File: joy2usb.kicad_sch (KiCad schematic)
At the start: 14 parts, among them J1 DB9_Male, J2 Conn_02x04_Odd_Even, SW1 RST, SW2 SW_SPDT, U1 Arduino_Pro_Micro, U2 4066

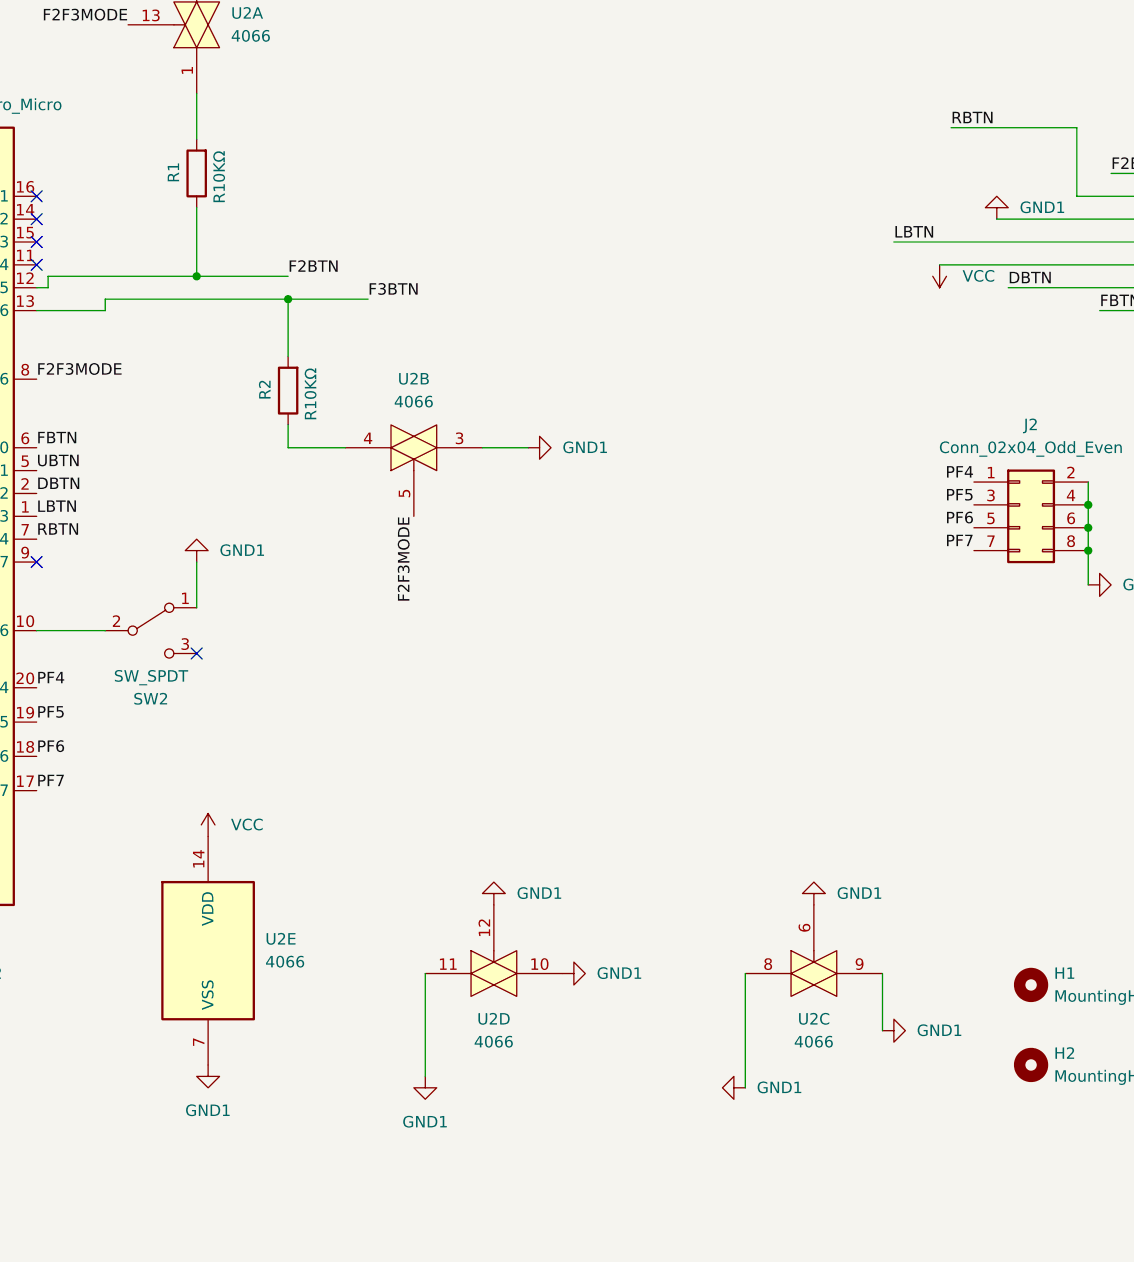
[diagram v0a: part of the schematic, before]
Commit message: PCB Rev. 2.0
Diode D1 is turned on in the same way as PULL-DOWN for the C64 Mode. Thus when D1 is on it means that PULL-DOWN for the C64 Mode is on, too.
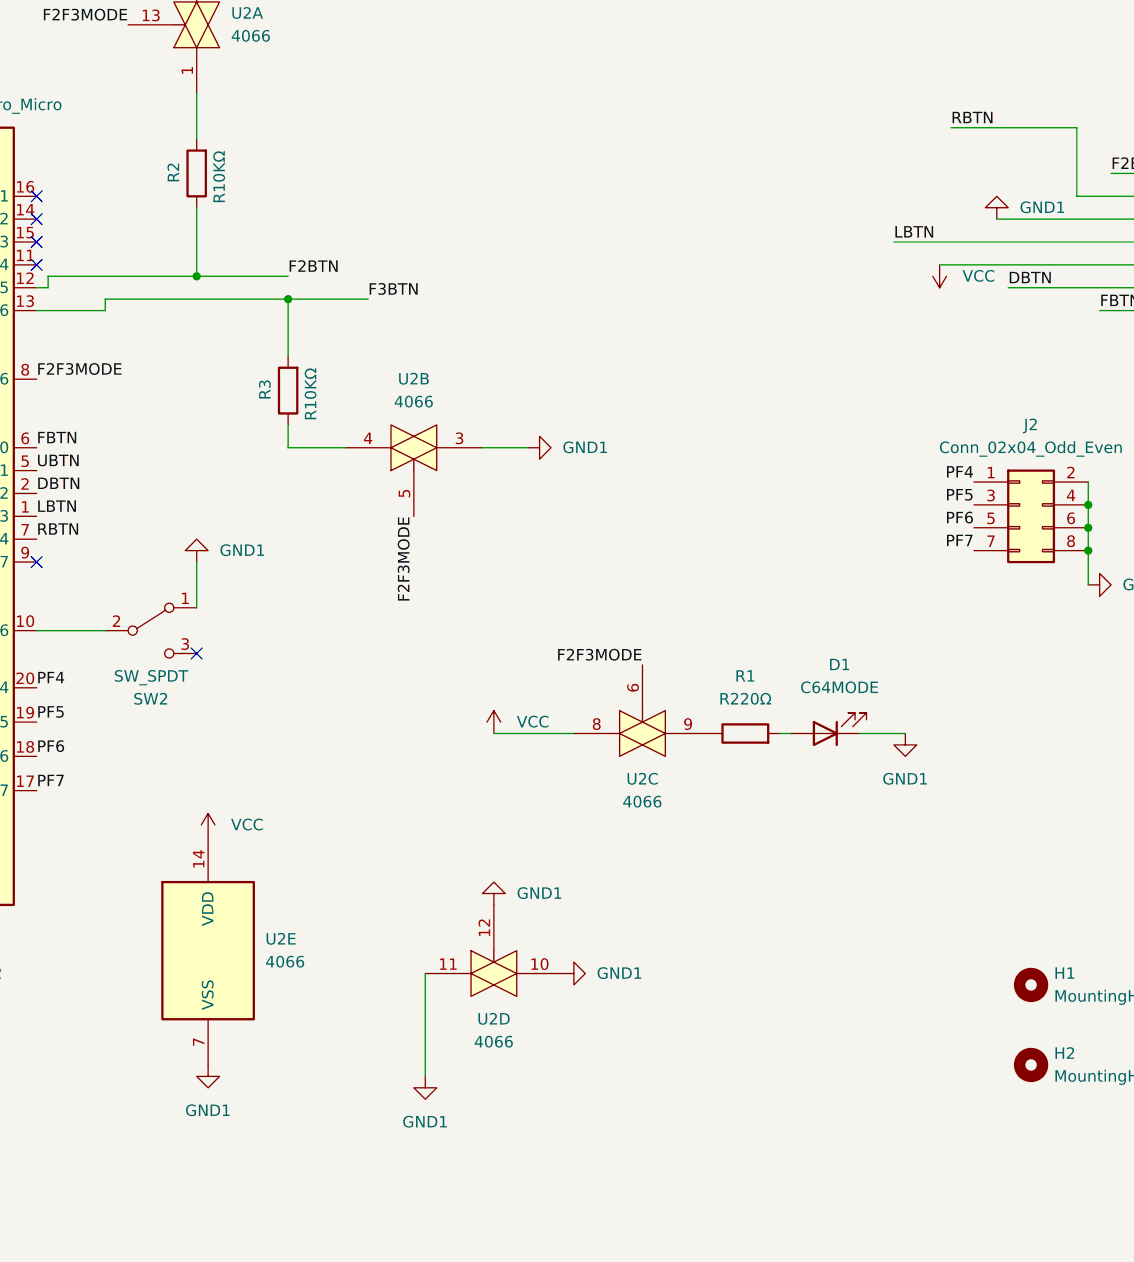
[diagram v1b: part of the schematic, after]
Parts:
- added D1: C64MODE, LED_THT:LED_D4.0mm, symbol Device:LED
- added R1: R220Ω, Resistor_THT:R_Axial_DIN0207_L6.3mm_D2.5mm_P10.16mm_Horizontal, symbol Device:R
- renumbered R1 to R2, R2 to R3
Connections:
- net F2F3MODE: now also U2.6
- net GND1: now also D1.1 (K); no longer U2.6, U2.8, U2.9
- net VCC: now also U2.8
- new net: R1.1, U2.9
- new net: D1.2 (A), R1.2

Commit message: PCB Rev. 2.3
Update of footprints -- oval pads
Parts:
- J1: footprint Connector_Dsub:DSUB-9_Male_Horizontal_P2.77x2.84mm_EdgePinOffset9.90mm_Housed_MountingHolesOffset11.32mm -> Misc:DSUB-9_Male_Horizontal_P2.77x2.84mm_EdgePinOffset9.90mm_Housed_OVAL_MountingHolesOffset11.32mm
- SW2: footprint Misc:MFP_1220_KNITTER_SWITCH_SPDT -> Misc:MFP_1220_KNITTER_SWITCH_SPDT_Oval
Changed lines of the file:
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@@
     (property "Reference" "SW2" (id 0) (at 124.46 106.68 0))
     (property "Value" "SW_SPDT" (id 1) (at 124.46 104.14 0))
-    (property "Footprint" "Misc:MFP_1220_KNITTER_SWITCH_SPDT" (id 2) (at 124.46 99.06 0)
+    (property "Footprint" "Misc:MFP_1220_KNITTER_SWITCH_SPDT_Oval" (id 2) (at 124.46 99.06 0)
       (effects (font (size 1.27 1.27)) hide)
     )
@@
       (effects (font (size 1.27 1.27)) (justify left))
     )
-    (property "Footprint" "Connector_Dsub:DSUB-9_Male_Horizontal_P2.77x2.84mm_EdgePinOffset9.90mm_Housed_MountingHolesOffset11.32mm" (id 2) (at 246.38 55.88 0)
+    (property "Footprint" "Misc:DSUB-9_Male_Horizontal_P2.77x2.84mm_EdgePinOffset9.90mm_Housed_OVAL_MountingHolesOffset11.32mm" (id 2) (at 246.38 55.88 0)
       (effects (font (size 1.27 1.27)) hide)
     )
@@
     )
     (path "/904b9dce-e0fa-4996-95ed-5106b4f66a12"
-      (reference "J1") (unit 1) (value "DB9_Male") (footprint "Connector_Dsub:DSUB-9_Male_Horizontal_P2.77x2.84mm_EdgePinOffset9.90mm_Housed_MountingHolesOffset11.32mm")
+      (reference "J1") (unit 1) (value "DB9_Male") (footprint "Misc:DSUB-9_Male_Horizontal_P2.77x2.84mm_EdgePinOffset9.90mm_Housed_OVAL_MountingHolesOffset11.32mm")
     )
     (path "/aa99628a-edde-4438-a929-0fc1f87b7e93"
@@
     )
     (path "/0dcce0bd-aa77-40a7-aa11-13358cb7d8b3"
-      (reference "SW2") (unit 1) (value "SW_SPDT") (footprint "Misc:MFP_1220_KNITTER_SWITCH_SPDT")
+      (reference "SW2") (unit 1) (value "SW_SPDT") (footprint "Misc:MFP_1220_KNITTER_SWITCH_SPDT_Oval")
     )
     (path "/5402cd64-4343-4e58-a540-d14fb99563fb"

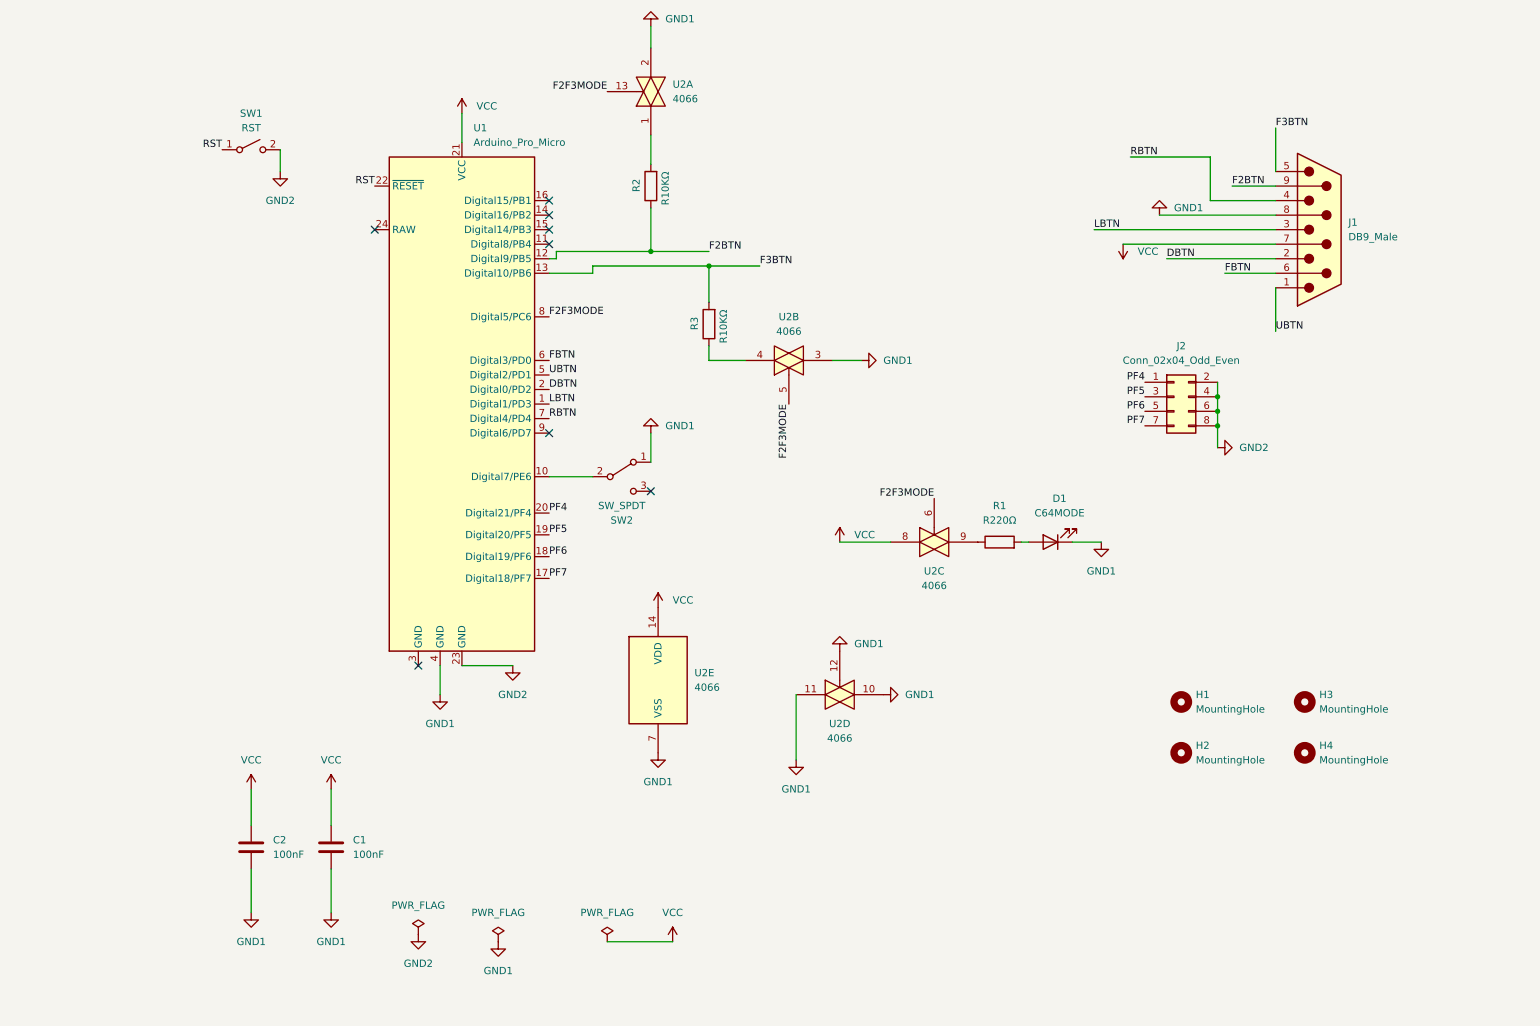
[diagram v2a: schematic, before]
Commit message: PCB Rev. 2.5
Update of LED footprint
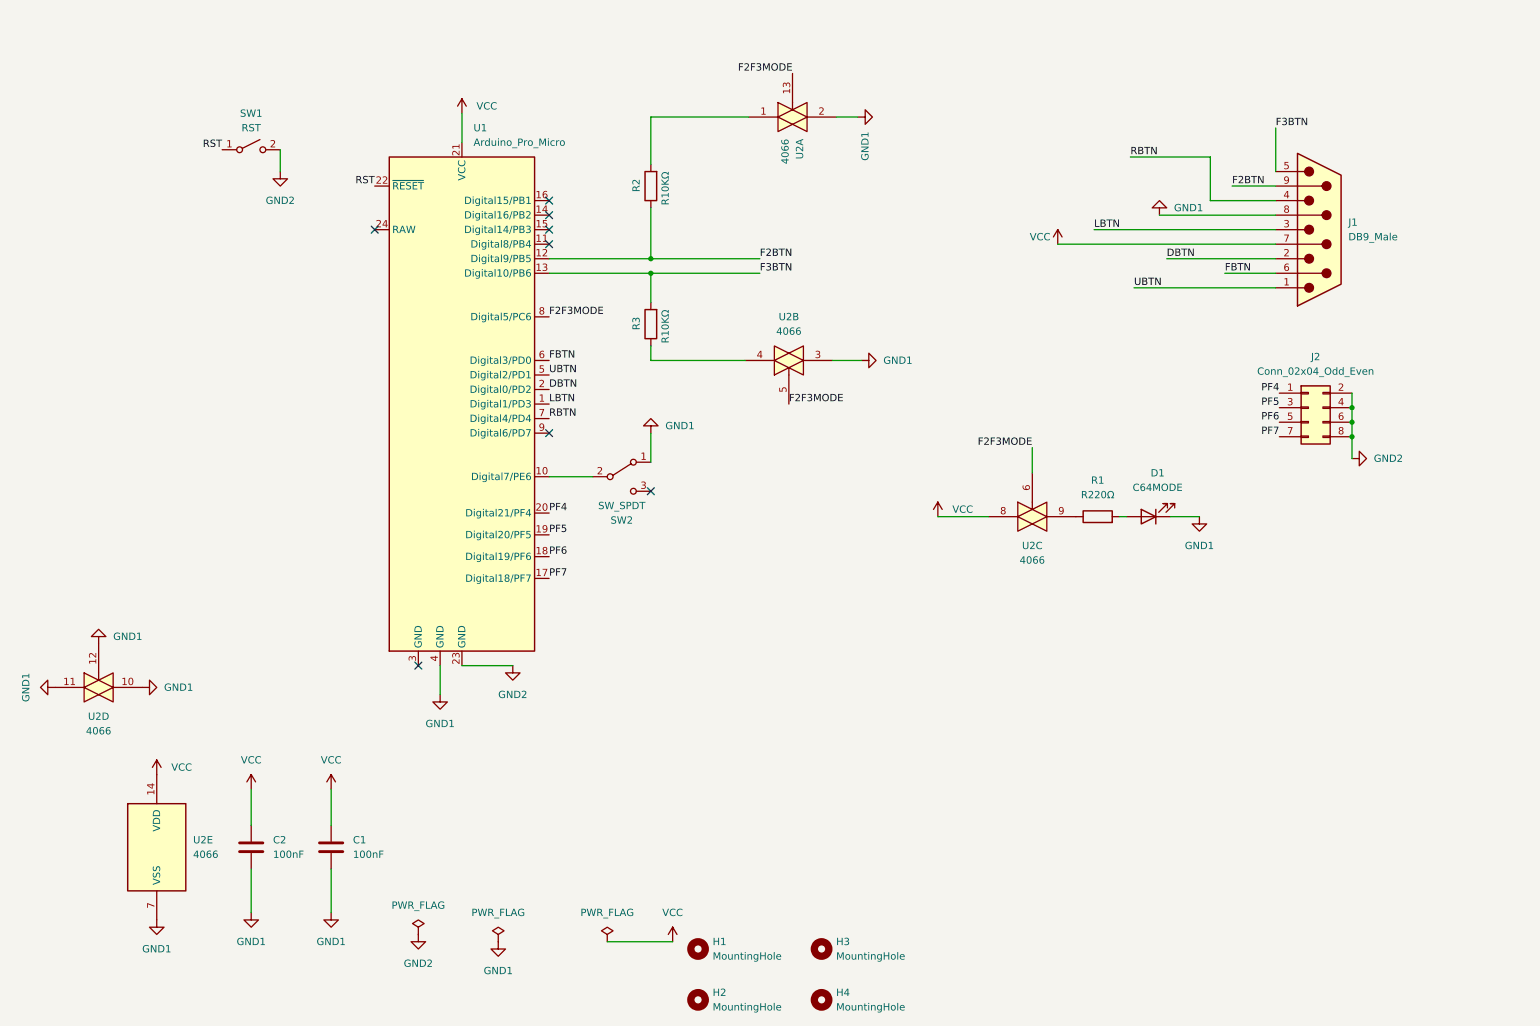
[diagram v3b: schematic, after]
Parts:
- D1: footprint LED_THT:LED_D4.0mm -> Misc:LED_D3.0mm_Oval
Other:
- moved on the sheet: D1, H1, H2, H3, H4, J2, R1, R3, U2A, U2C, U2D, U2E

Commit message: PCB Rev. 3.0
Replace GND1 and GND2 with GND.
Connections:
- net GND1 is gone; now on net GND: C1.2, C2.2, D1.1 (K), J1.8, SW2.1 (A), U1.4 (GND), U2.10, U2.11, U2.12, U2.2, U2.3, U2.7 (VSS)
- net GND2 is gone; now on net GND: J2.2 (Pin_2), J2.4 (Pin_4), J2.6 (Pin_6), J2.8 (Pin_8), SW1.2 (B), U1.23 (GND)
- net GND: now reaches U1.3 (GND)
- no-connect marks 8 -> 7
